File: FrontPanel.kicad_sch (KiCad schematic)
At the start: 8 parts, among them SW1 RST, U26 ESP32-C3-MINI-1

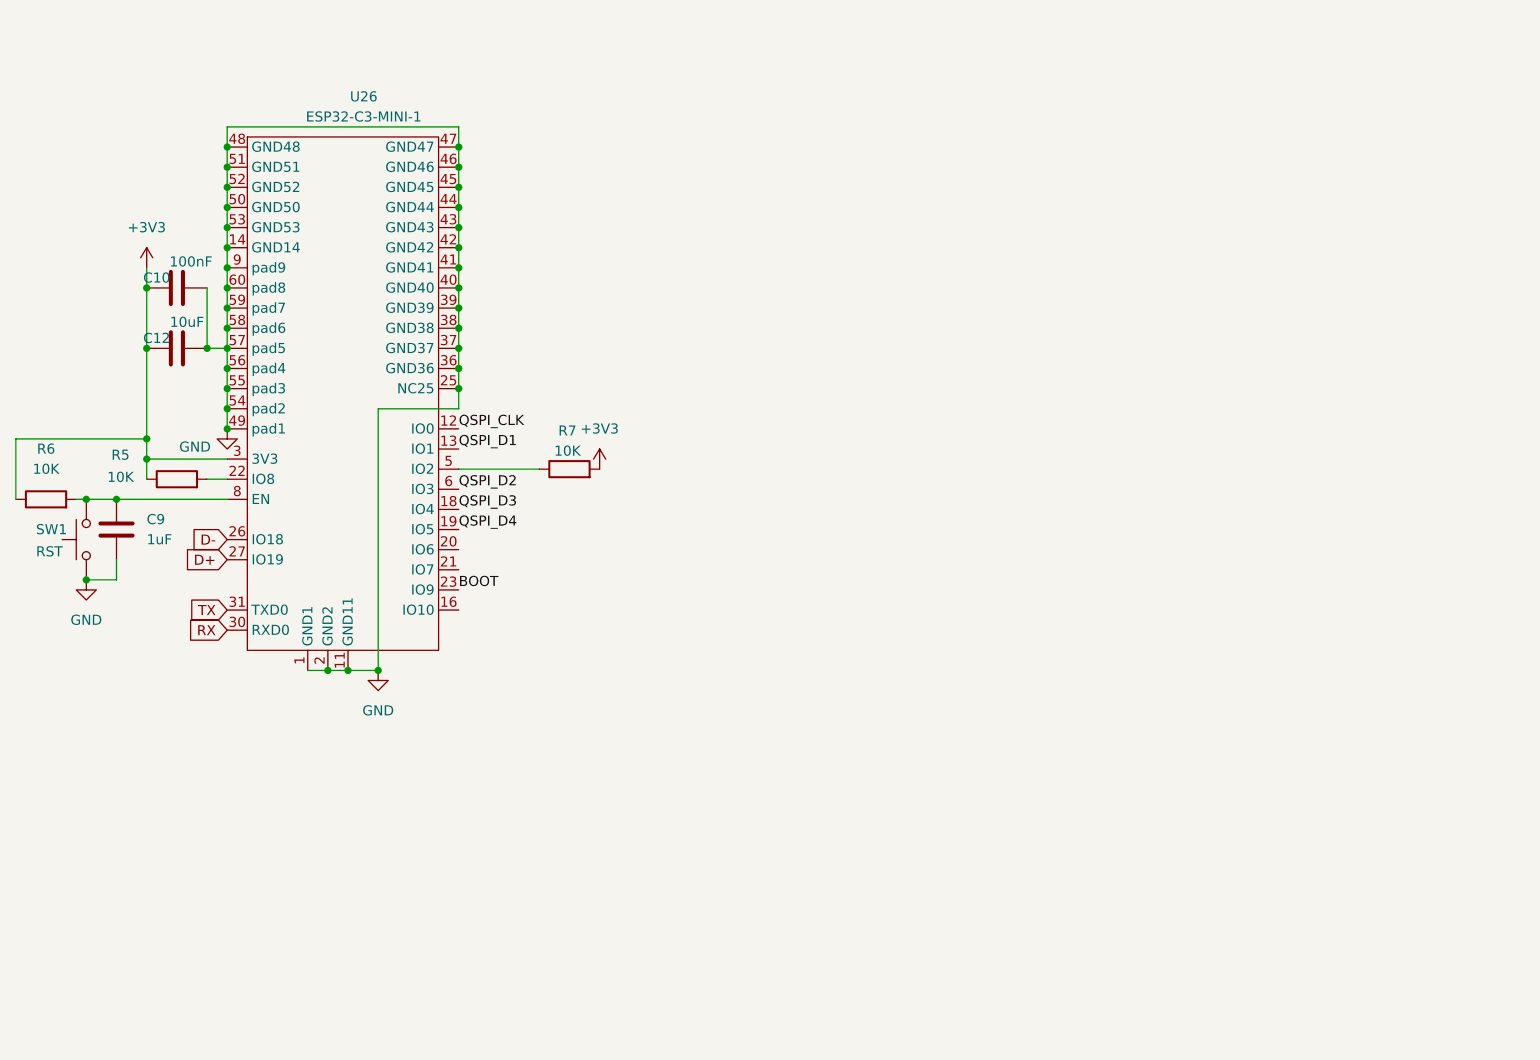
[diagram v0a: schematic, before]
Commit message: update
break down schemantic to panels, added controller and additional commponents, fixed
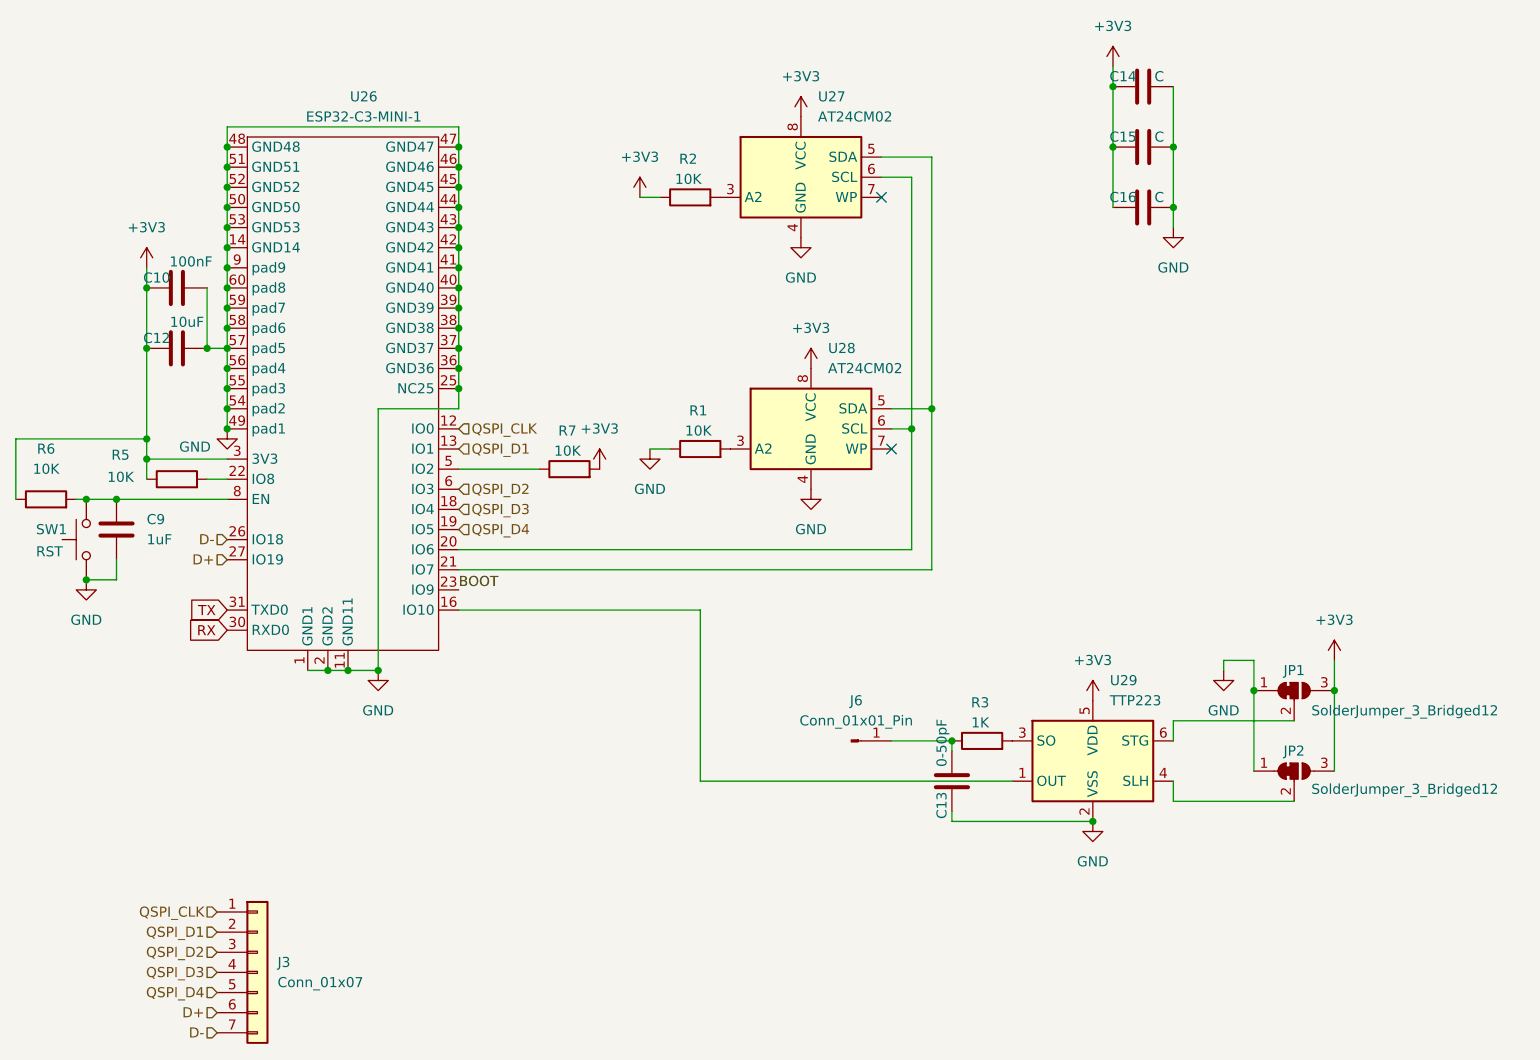
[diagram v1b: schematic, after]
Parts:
- added C13: 0-50pF, Capacitor_SMD:C_0603_1608Metric, symbol Device:C
- added C14, C15, C16: C, Capacitor_SMD:C_0603_1608Metric, symbol Device:C
- added J3: Conn_01x07, Connector_PinHeader_2.54mm:PinHeader_1x07_P2.54mm_Vertical, symbol Connector_Generic:Conn_01x07
- added J6: Conn_01x01_Pin, Connector_PinSocket_2.54mm:PinSocket_1x01_P2.54mm_Vertical, symbol Connector:Conn_01x01_Pin
- added JP1, JP2: SolderJumper_3_Bridged12, MyLib:LittleSolderJumper, symbol Jumper:SolderJumper_3_Bridged12
- added R1, R2: 10K, Resistor_SMD:R_0603_1608Metric, symbol Device:R
- added R3: 1K, Resistor_SMD:R_0603_1608Metric, symbol Device:R
- added U27, U28: AT24CM02, Package_SO:SOP-8_3.76x4.96mm_P1.27mm, symbol EEPROM:AT24CM02
- added U29: TTP223, Package_TO_SOT_SMD:SOT-23-6, symbol Touch:TTP223
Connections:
- net +3V3: now also C14.1, C15.1, C16.1, JP1.3 (B), JP2.3 (B), R2.1, U27.8 (VCC), U28.8 (VCC), U29.5 (VDD)
- net D+: now also J3.6 (Pin_6)
- net D-: now also J3.7 (Pin_7)
- net GND: now also C13.1, C14.2, C15.2, C16.2, JP1.1 (A), JP2.1 (A), R1.1, U27.4 (GND), U28.4 (GND), U29.2 (VSS)
- net QSPI_CLK: now also J3.1 (Pin_1)
- net QSPI_D1: now also J3.2 (Pin_2)
- net QSPI_D2: now also J3.3 (Pin_3)
- net QSPI_D3: now also J3.4 (Pin_4)
- net QSPI_D4: now also J3.5 (Pin_5)
- net at U26.16 (IO10): now also U29.1 (OUT)
- net at U26.20 (IO6): now also U27.6 (SCL), U28.6 (SCL)
- net at U26.21 (IO7): now also U27.5 (SDA), U28.5 (SDA)
- new net: R1.2, U28.3 (A2)
- new net: R2.2, U27.3 (A2)
- new net: R3.2, U29.3 (SO)
- new net: JP2.2 (C), U29.4 (SLH)
- new net: JP1.2 (C), U29.6 (STG)
- new net: C13.2, J6.1 (Pin_1), R3.1
- no-connect marks 0 -> 2
